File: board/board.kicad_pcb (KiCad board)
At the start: 2 copper layers, 50 x 81 mm, 62 parts, among them IC1 tps610986, IC2 LTR-303ALS-01, IC3 EFM32TG108F32, J1 Conn_01x05_Male, J2 Conn_01x04_Female, SW1 SW_Push, Y1 Crystal

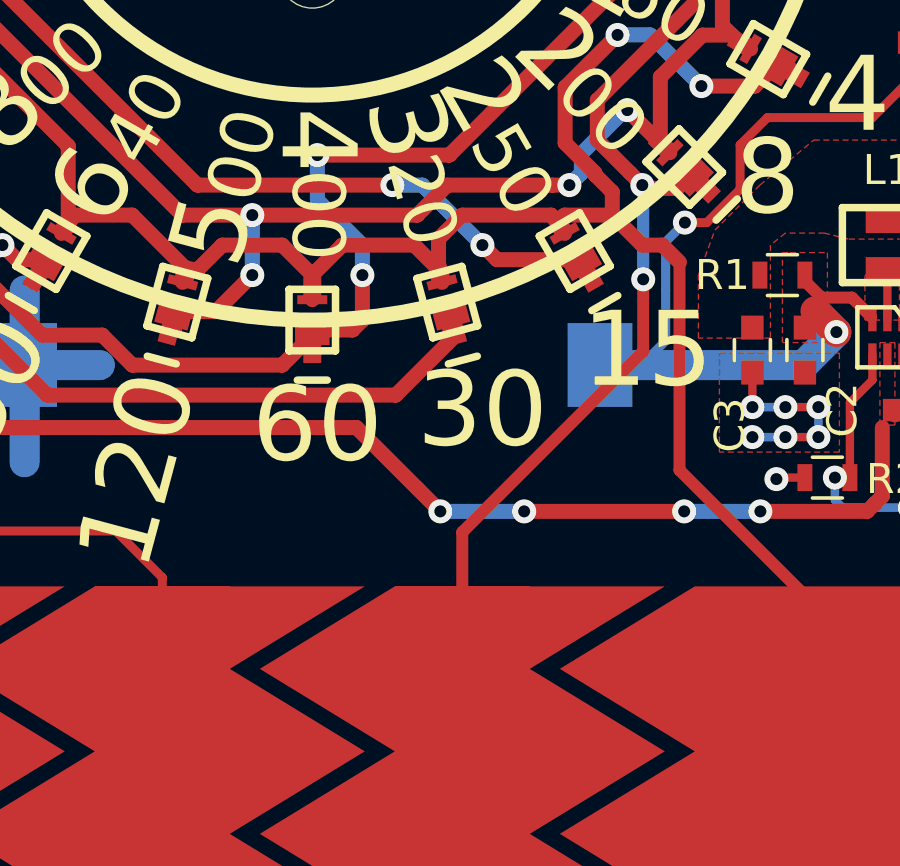
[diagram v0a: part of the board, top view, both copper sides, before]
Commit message: capsense tweak
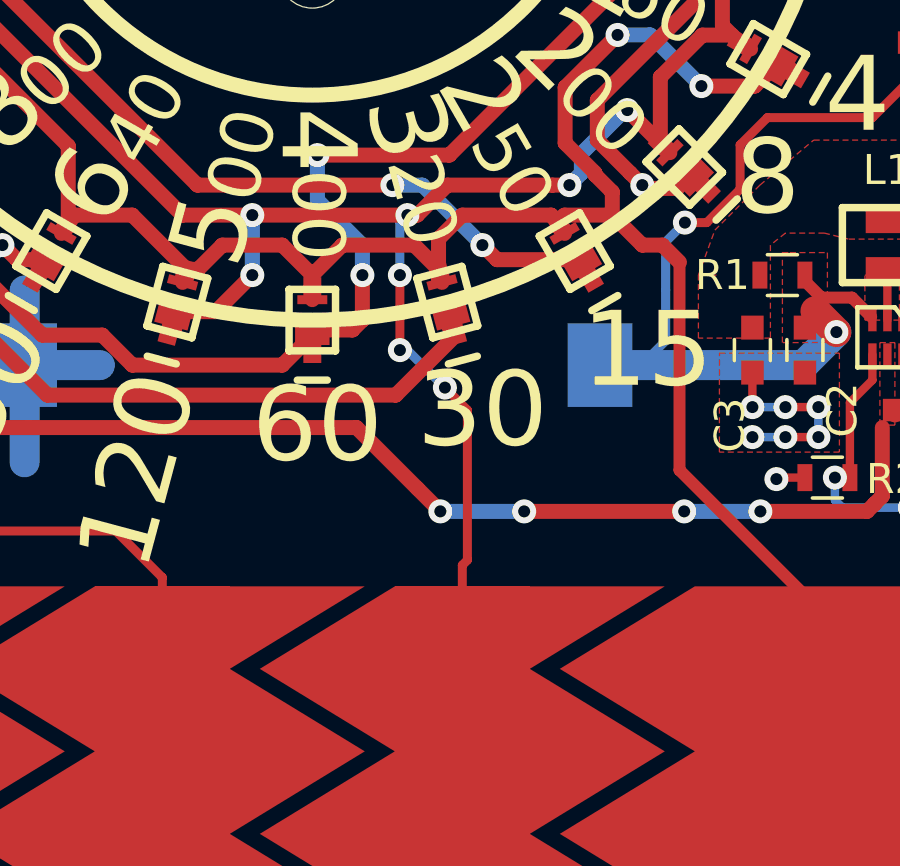
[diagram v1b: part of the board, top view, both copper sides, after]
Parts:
- R1: value 400 -> 402
- R3, R4: value 11k -> 10k
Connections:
- J2 pad 3: DPIN6 -> DPIN5
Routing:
- net DPIN6: track 190.2 -> 157.2 mm, vias 10 -> 9
- net DPIN5: track 151.0 -> 181.5 mm, vias 10 -> 14

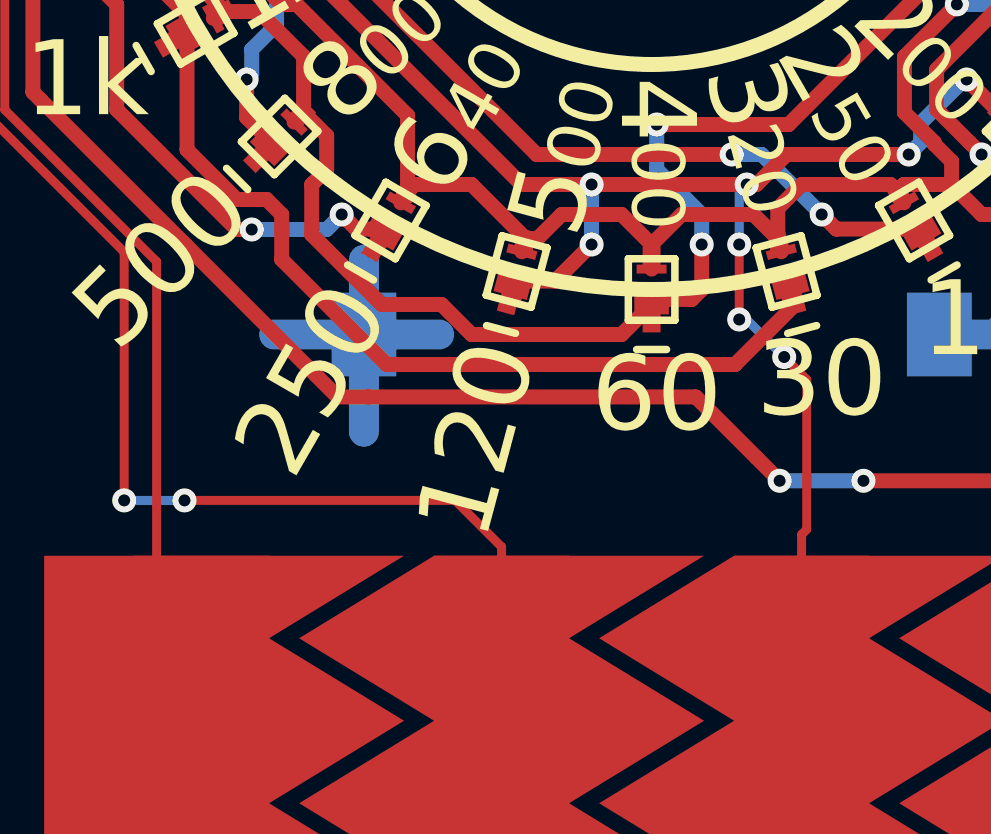
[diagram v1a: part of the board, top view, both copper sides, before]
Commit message: Alternate diode / non-diode slider pins
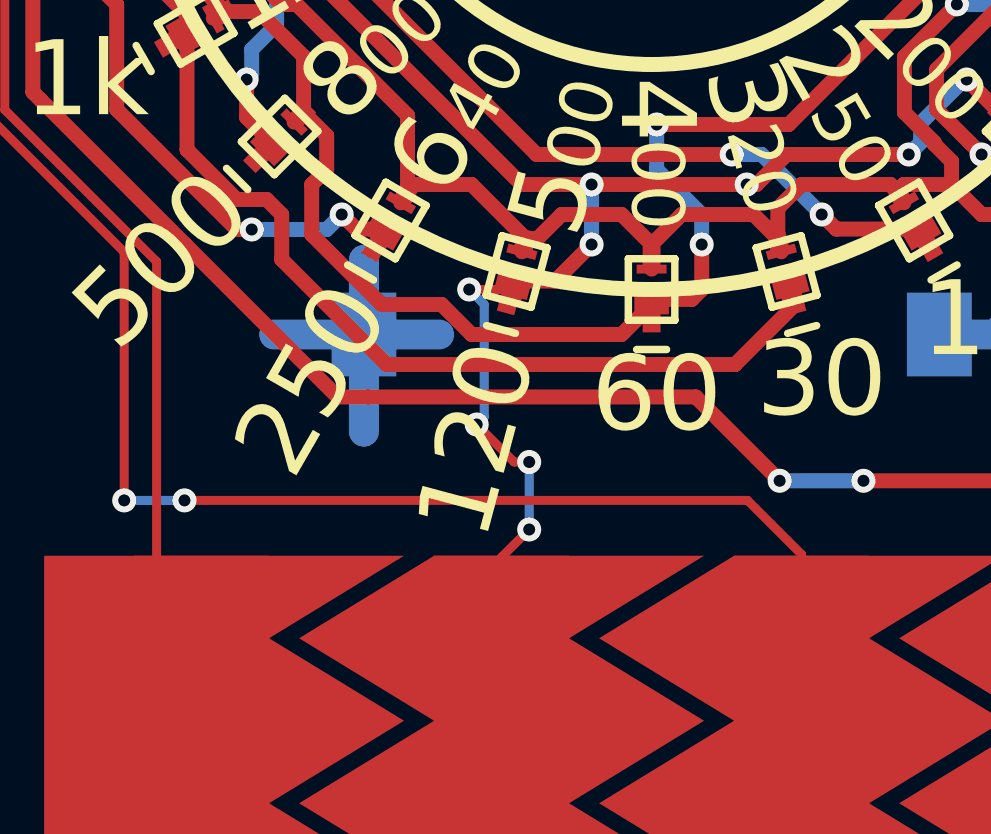
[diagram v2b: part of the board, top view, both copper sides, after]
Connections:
- IC3 pad 4: S2 -> S3
- J2 pad 2: S2 -> DPIN5
- J2 pad 3: DPIN5 -> S3
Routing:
- net S3: track 0.00 -> 109.4 mm, vias 0 -> 6
- net S2: track 99.9 -> 0.00 mm, vias 6 -> 0
- net DPIN5: track 181.5 -> 180.0 mm, vias 14 -> 15

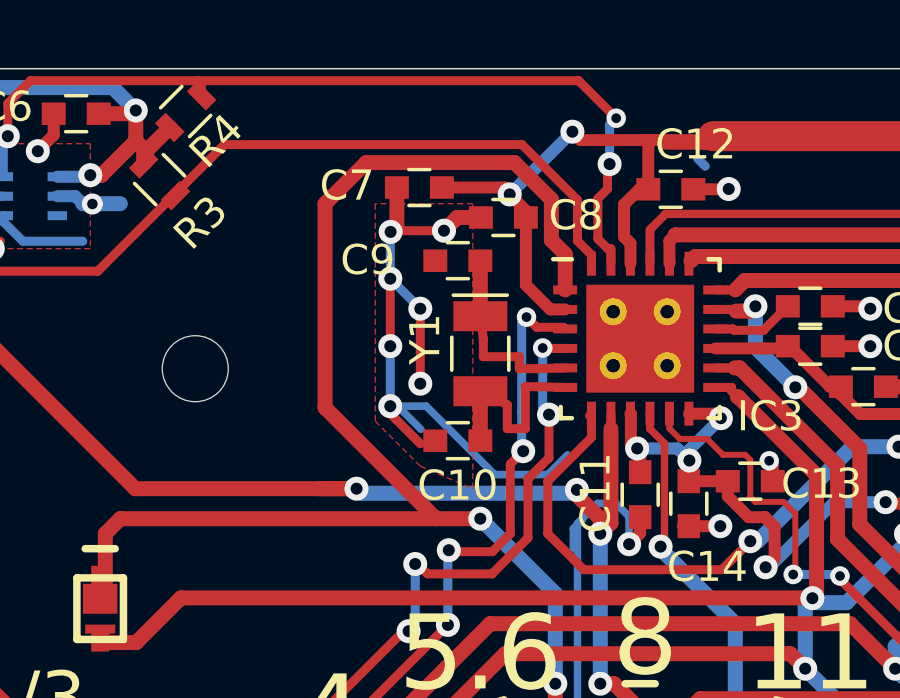
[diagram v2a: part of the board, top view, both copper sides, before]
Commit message: Remove crystal
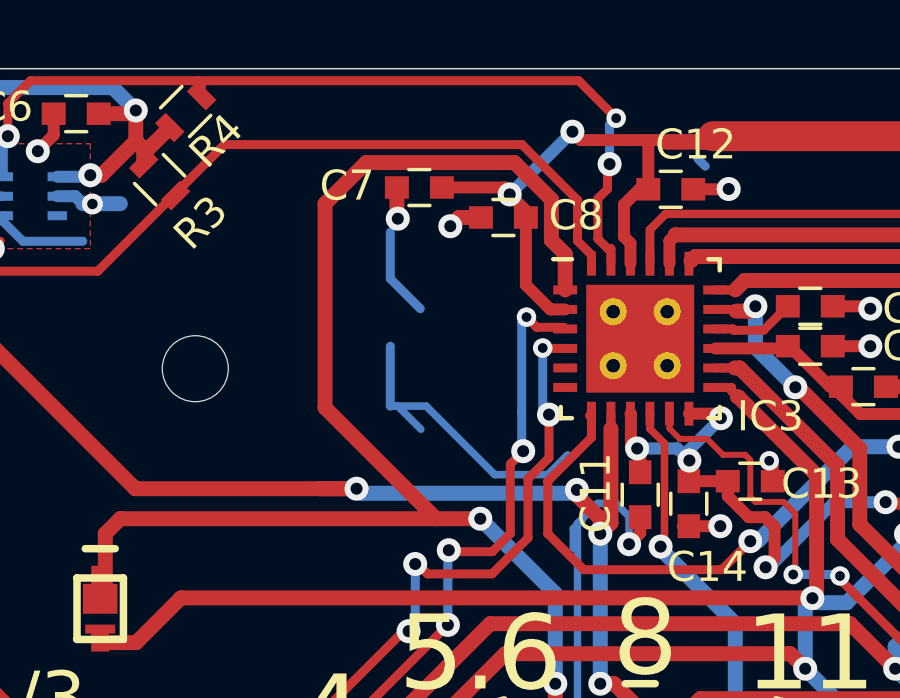
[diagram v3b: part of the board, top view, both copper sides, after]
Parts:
- removed C10, C9: 12p5, Capacitors_SMD:C_0603
- removed Y1: Crystal, Crystals:Crystal_SMD_MicroCrystal_CC7V-T1A-2pin_3.2x1.5mm
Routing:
- net GND: track 79.7 -> 70.7 mm, vias 35 -> 30
- net Net-(IC3-Pad6): track 6.79 -> 0.00 mm
- net Net-(IC3-Pad5): track 6.34 -> 0.00 mm

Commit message: initial work on rewiring following crystal removal
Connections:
- IC3 pad 17: DPIN4 -> S4
- IC3 pad 18: DPIN5 -> S2
- IC3 pad 5: Net-(IC3-Pad5) -> DPIN5
- IC3 pad 6: Net-(IC3-Pad6) -> DPIN6
- J2 pad 2: DPIN5 -> S2
- J2 pad 4: DPIN4 -> S4
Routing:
- net DPIN5: track 180.0 -> 133.8 mm
- net DPIN4: track 181.6 -> 164.9 mm, vias 11 -> 8

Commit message: Minor
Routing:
- net DPIN4: track 164.9 -> 134.1 mm
- net S4: track 0.00 -> 20.3 mm
- net DPIN5: track 133.8 -> 117.1 mm
- net S2: track 0.00 -> 14.1 mm
- net S1: track 77.4 -> 64.5 mm
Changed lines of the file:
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@@
     (thickness 1.6)
     (drawings 75)
-    (tracks 1010)
+    (tracks 1005)
     (zones 0)
     (modules 59)
@@
   )
   (setup
-    (last_trace_width 0.5)
+    (last_trace_width 0.3)
     (user_trace_width 0.2)
     (user_trace_width 0.28)
@@
   (via (at 97.12 83.175) (size 0.8) (drill 0.4) (layers F.Cu B.Cu) (net 2))
   (segment (start 82.67 75) (end 93.195 75) (width 0.5) (layer F.Cu) (net 2))
-  (segment (start 100.5 129.5) (end 105 129.5) (width 0.25) (layer F.Cu) (net 28))
-  (segment (start 100.5 135) (end 105 135) (width 0.25) (layer F.Cu) (net 28))
-  (segment (start 105 133.125) (end 107.25 130.875) (width 0.25) (layer F.Cu) (net 28))
-  (segment (start 105 135) (end 105 133.125) (width 0.25) (layer F.Cu) (net 28))
   (segment (start 97.5 66.178542) (end 97.5 67.375) (width 0.5) (layer F.Cu) (net 2))
   (segment (start 97.04 65.718542) (end 97.5 66.178542) (width 0.5) (layer F.Cu) (net 2))
@@
   (segment (start 86.655788 84.514212) (end 80.67 90.5) (width 0.5) (layer F.Cu) (net 5))
   (segment (start 91.135 84.514212) (end 86.655788 84.514212) (width 0.5) (layer F.Cu) (net 5))
-  (segment (start 110.5 129.5) (end 116.5 129.5) (width 0.25) (layer F.Cu) (net 5))
-  (segment (start 116.5 129.5) (end 116.5 135) (width 0.25) (layer F.Cu) (net 5))
-  (segment (start 111 129.5) (end 116.5 135) (width 0.4) (layer F.Cu) (net 5))
-  (segment (start 110.5 129.5) (end 111 129.5) (width 0.4) (layer F.Cu) (net 5))
-  (segment (start 111 135) (end 116.5 129.5) (width 0.4) (layer F.Cu) (net 5))
-  (segment (start 110.5 135) (end 111 135) (width 0.4) (layer F.Cu) (net 5))
   (segment (start 108.428002 109.741998) (end 110.175019 107.994981) (width 0.5) (layer F.Cu) (net 5))
   (segment (start 109.420001 112.591999) (end 108.428002 111.6) (width 0.5) (layer F.Cu) (net 5))
@@
   (segment (start 112.24 122.5) (end 112.24 115.57) (width 0.4) (layer F.Cu) (net 5))
   (segment (start 116.5 126.76) (end 112.24 122.5) (width 0.4) (layer F.Cu) (net 5))
-  (segment (start 116.5 129.5) (end 116.5 126.76) (width 0.4) (layer F.Cu) (net 5))
   (segment (start 111 115) (end 111.67 115) (width 0.5) (layer F.Cu) (net 5))
   (segment (start 111.600969 111.600969) (end 111.600969 109.399031) (width 0.5) (layer F.Cu) (net 6))
@@
   (segment (start 102.72 76.7) (end 98.12 76.7) (width 0.3) (layer F.Cu) (net 15))
   (segment (start 103.67 75.75) (end 102.72 76.7) (width 0.3) (layer F.Cu) (net 15))
-  (segment (start 90.5 129.5) (end 95 129.5) (width 0.25) (layer F.Cu) (net 6))
-  (segment (start 90.5 135) (end 95 135) (width 0.25) (layer F.Cu) (net 6))
-  (segment (start 95 131.375) (end 97.25 133.625) (width 0.25) (layer F.Cu) (net 6))
-  (segment (start 95 129.5) (end 95 131.375) (width 0.25) (layer F.Cu) (net 6))
   (via (at 95.92 125.5) (size 0.8) (drill 0.4) (layers F.Cu B.Cu) (net 6))
   (segment (start 95 126.42) (end 95.92 125.5) (width 0.3) (layer F.Cu) (net 6))
-  (segment (start 95 129.125) (end 95 126.42) (width 0.3) (layer F.Cu) (net 6))
   (via (at 95.92 123.25) (size 0.8) (drill 0.4) (layers F.Cu B.Cu) (net 6))
   (segment (start 95.92 125.5) (end 95.92 123.25) (width 0.3) (layer B.Cu) (net 6))
@@
   (via (at 93.67 65.25) (size 0.8) (drill 0.4) (layers F.Cu B.Cu) (net 10))
   (segment (start 94.69 64.96) (end 93.96 64.96) (width 0.5) (layer F.Cu) (net 10))
+  (segment (start 90.5 129.125) (end 95 129.125) (width 0.3) (layer F.Cu) (net 16))
+  (segment (start 90.5 134.625) (end 95 134.625) (width 0.3) (layer F.Cu) (net 16))
+  (segment (start 95 131) (end 97.25 133.25) (width 0.3) (layer F.Cu) (net 16))
+  (segment (start 95 129.125) (end 95 131) (width 0.3) (layer F.Cu) (net 16))
   (segment (start 96.765 69.325) (end 97.5 69.325) (width 0.3) (layer F.Cu) (net 28))
   (segment (start 96.75 69.31) (end 96.765 69.325) (width 0.3) (layer F.Cu) (net 28))
@@
   (segment (start 92.5 76.51) (end 92.58 76.51) (width 0.3) (layer F.Cu) (net 28))
   (segment (start 92.58 76.51) (end 92.91 76.84) (width 0.3) (layer F.Cu) (net 28))
-  (segment (start 87.25 130.875) (end 87.25 133.625) (width 0.25) (layer F.Cu) (net 17))
   (via (at 96.21 68.28) (size 0.65) (drill 0.325) (layers F.Cu B.Cu) (net 17))
   (segment (start 97.445 68.62) (end 97.5 68.675) (width 0.3) (layer F.Cu) (net 17))
@@
   (segment (start 82.73 87.05) (end 82.73 87.04) (width 0.3) (layer F.Cu) (net 17))
   (segment (start 78.44 111.51) (end 78.44 91.34) (width 0.3) (layer F.Cu) (net 17))
-  (segment (start 83.5 129.5) (end 83.5 116.57) (width 0.3) (layer F.Cu) (net 17))
   (segment (start 95.67 73.18) (end 96.1 72.75) (width 0.3) (layer F.Cu) (net 17))
   (segment (start 95.67 75.5) (end 95.67 73.18) (width 0.3) (layer F.Cu) (net 17))
@@
   (segment (start 93.67 76.1) (end 95.07 76.1) (width 0.3) (layer F.Cu) (net 17))
   (segment (start 93.62 76.05) (end 93.67 76.1) (width 0.3) (layer F.Cu) (net 17))
+  (segment (start 87.25 130.5) (end 87.25 133.25) (width 0.3) (layer F.Cu) (net 17))
   (segment (start 100 73.45) (end 100 72.94) (width 0.4) (layer F.Cu) (net 19))
   (segment (start 99.69 71.515) (end 99.675 71.5) (width 0.4) (layer F.Cu) (net 19))
@@
   (segment (start 84.43 124.53) (end 82.42 124.53) (width 0.3) (layer B.Cu) (net 28))
   (via (at 84.43 124.53) (size 0.8) (drill 0.4) (layers F.Cu B.Cu) (net 28))
-  (segment (start 105 126.33) (end 105 129.125) (width 0.3) (layer F.Cu) (net 28))
-  (segment (start 103.2 124.53) (end 105 126.33) (width 0.3) (layer F.Cu) (net 28))
-  (segment (start 84.43 124.53) (end 103.2 124.53) (width 0.3) (layer F.Cu) (net 28))
+  (segment (start 100.5 129.125) (end 105 129.125) (width 0.3) (layer F.Cu) (net 28))
+  (segment (start 100.5 134.625) (end 105 134.625) (width 0.3) (layer F.Cu) (net 28))
+  (segment (start 103.2 124.53) (end 84.43 124.53) (width 0.3) (layer F.Cu) (net 28))
+  (segment (start 105 126.33) (end 103.2 124.53) (width 0.3) (layer F.Cu) (net 28))
+  (segment (start 105 129.125) (end 105 126.33) (width 0.3) (layer F.Cu) (net 28))
+  (segment (start 105 131) (end 107.25 133.25) (width 0.3) (layer F.Cu) (net 28))
+  (segment (start 105 129.125) (end 105 131) (width 0.3) (layer F.Cu) (net 28))
+  (segment (start 110.5 129.125) (end 116.5 129.125) (width 0.3) (layer F.Cu) (net 29))
+  (segment (start 110.5 134.625) (end 116.5 134.625) (width 0.3) (layer F.Cu) (net 29))
+  (segment (start 111 129.125) (end 116.5 134.625) (width 0.3) (layer F.Cu) (net 29))
+  (segment (start 110.5 129.125) (end 111 129.125) (width 0.3) (layer F.Cu) (net 29))
   (zone (net 10) (net_name GND) (layer B.Cu) (hatch edge 0.508)
     (connect_pads (clearance 0.508))

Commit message: Minor
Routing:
- net DPIN4: track 134.1 -> 117.8 mm
- net S1: track 64.5 -> 77.0 mm
- net GND: track 70.7 -> 60.0 mm
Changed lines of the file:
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@@
     (thickness 1.6)
     (drawings 75)
-    (tracks 1005)
+    (tracks 994)
     (zones 0)
     (modules 59)
@@
     (36 B.SilkS user)
     (37 F.SilkS user hide)
-    (38 B.Mask user)
-    (39 F.Mask user)
+    (38 B.Mask user hide)
+    (39 F.Mask user hide)
     (40 Dwgs.User user)
     (41 Cmts.User user)
@@
   (segment (start 82.21556 104.58541) (end 82.008504 104.792466) (width 0.5) (layer F.Cu) (net 5))
   (segment (start 82.781244 104.58541) (end 82.21556 104.58541) (width 0.5) (layer F.Cu) (net 5))
-  (segment (start 111 115) (end 110 114) (width 0.5) (layer F.Cu) (net 5))
-  (segment (start 108.406391 114) (end 108.185 114.221391) (width 0.5) (layer F.Cu) (net 5))
-  (segment (start 110 114) (end 108.406391 114) (width 0.5) (layer F.Cu) (net 5))
   (segment (start 108.185 114.386103) (end 108.41 114.611103) (width 0.5) (layer F.Cu) (net 5))
   (segment (start 108.185 114.221391) (end 108.185 114.386103) (width 0.5) (layer F.Cu) (net 5))
@@
   (segment (start 86.655788 84.514212) (end 80.67 90.5) (width 0.5) (layer F.Cu) (net 5))
   (segment (start 91.135 84.514212) (end 86.655788 84.514212) (width 0.5) (layer F.Cu) (net 5))
-  (segment (start 108.428002 109.741998) (end 110.175019 107.994981) (width 0.5) (layer F.Cu) (net 5))
-  (segment (start 109.420001 112.591999) (end 108.428002 111.6) (width 0.5) (layer F.Cu) (net 5))
-  (segment (start 108.428002 111.6) (end 108.428002 109.741998) (width 0.5) (layer F.Cu) (net 5))
-  (segment (start 109.420001 112.650001) (end 109.420001 112.591999) (width 0.5) (layer F.Cu) (net 5))
-  (segment (start 110 113.23) (end 109.420001 112.650001) (width 0.5) (layer F.Cu) (net 5))
-  (segment (start 110 114) (end 110 113.23) (width 0.5) (layer F.Cu) (net 5))
   (via (at 110.175019 107.994981) (size 0.8) (drill 0.4) (layers F.Cu B.Cu) (net 5))
   (segment (start 111.264981 107.994981) (end 112.97 109.7) (width 0.5) (layer B.Cu) (net 5))
@@
   (segment (start 114.750788 109.7) (end 115.485788 108.965) (width 0.5) (layer F.Cu) (net 5))
   (segment (start 112.97 109.7) (end 114.750788 109.7) (width 0.5) (layer F.Cu) (net 5))
-  (segment (start 112.24 115.57) (end 111.67 115) (width 0.5) (layer F.Cu) (net 5))
-  (segment (start 112.24 122.5) (end 112.24 115.57) (width 0.4) (layer F.Cu) (net 5))
-  (segment (start 116.5 126.76) (end 112.24 122.5) (width 0.4) (layer F.Cu) (net 5))
-  (segment (start 111 115) (end 111.67 115) (width 0.5) (layer F.Cu) (net 5))
+  (segment (start 108.428002 111.6) (end 108.428002 109.741998) (width 0.5) (layer F.Cu) (net 5))
+  (segment (start 109.420001 112.650001) (end 109.420001 112.591999) (width 0.5) (layer F.Cu) (net 5))
+  (segment (start 110 113.23) (end 109.420001 112.650001) (width 0.5) (layer F.Cu) (net 5))
+  (segment (start 109.420001 112.591999) (end 108.428002 111.6) (width 0.5) (layer F.Cu) (net 5))
+  (segment (start 109.17 114) (end 110 113.23) (width 0.5) (layer F.Cu) (net 5))
+  (segment (start 108.406391 114) (end 109.17 114) (width 0.5) (layer F.Cu) (net 5))
+  (segment (start 108.428002 109.741998) (end 110.175019 107.994981) (width 0.5) (layer F.Cu) (net 5))
+  (segment (start 108.185 114.221391) (end 108.406391 114) (width 0.5) (layer F.Cu) (net 5))
   (segment (start 111.600969 111.600969) (end 111.600969 109.399031) (width 0.5) (layer F.Cu) (net 6))
   (segment (start 111.600969 109.399031) (end 113 108) (width 0.5) (layer F.Cu) (net 6))
@@
   (via (at 78.42 66) (size 0.8) (drill 0.4) (layers F.Cu B.Cu) (net 10))
   (segment (start 78.67 65.75) (end 78.42 66) (width 0.3) (layer F.Cu) (net 10))
-  (segment (start 91.67 69.25) (end 91.67 71.25) (width 0.3) (layer B.Cu) (net 10))
-  (segment (start 91.67 67) (end 92.67 68) (width 0.3) (layer B.Cu) (net 10))
   (segment (start 90.41 119) (end 90.41 122.24) (width 1) (layer B.Cu) (net 10))
   (segment (start 90.41 119) (end 92.92 119) (width 1) (layer B.Cu) (net 10))
@@
   (segment (start 100 75.48) (end 99.63 75.85) (width 0.4) (layer F.Cu) (net 10))
   (segment (start 100 74.95) (end 100 75.48) (width 0.4) (layer F.Cu) (net 10))
-  (segment (start 91.67 65.45) (end 91.67 67) (width 0.3) (layer B.Cu) (net 10))
   (via (at 109.42 70.5) (size 0.8) (drill 0.4) (layers F.Cu B.Cu) (net 10))
   (segment (start 109.32 70.6) (end 109.42 70.5) (width 0.5) (layer F.Cu) (net 10))
@@
   (via (at 107.67 69.25) (size 0.8) (drill 0.4) (layers F.Cu B.Cu) (net 10))
   (segment (start 106.42 69.25) (end 107.67 69.25) (width 0.4) (layer F.Cu) (net 10))
-  (segment (start 91.67 71.25) (end 91.92 71.25) (width 0.25) (layer B.Cu) (net 10))
-  (segment (start 91.92 71.25) (end 92.69 72.02) (width 0.25) (layer B.Cu) (net 10))
-  (segment (start 91.67 71.25) (end 92.87 71.25) (width 0.25) (layer B.Cu) (net 10))
-  (segment (start 92.87 71.25) (end 95.15 73.53) (width 0.25) (layer B.Cu) (net 10))
   (segment (start 95.15 73.53) (end 96.92 73.53) (width 0.25) (layer B.Cu) (net 10))
   (segment (start 96.92 73.53) (end 97.58 72.87) (width 0.25) (layer B.Cu) (net 10))
@@
   (segment (start 93.62 76.05) (end 93.67 76.1) (width 0.3) (layer F.Cu) (net 17))
   (segment (start 87.25 130.5) (end 87.25 133.25) (width 0.3) (layer F.Cu) (net 17))
+  (segment (start 83.5 116.57) (end 83.5 129.125) (width 0.3) (layer F.Cu) (net 17))
   (segment (start 100 73.45) (end 100 72.94) (width 0.4) (layer F.Cu) (net 19))
   (segment (start 99.69 71.515) (end 99.675 71.5) (width 0.4) (layer F.Cu) (net 19))
